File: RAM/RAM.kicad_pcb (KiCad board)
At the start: 2 copper layers, 133 x 58.5 mm, 60 parts, among them J1 Conn_01x02_Pin, J2 Conn_01x01_Pin, J3 Conn_01x02_Pin, J4 Conn_01x01_Pin, J5 Conn_01x05_Pin, J6 Conn_01x03_Pin, J7 Conn_01x03_Pin, J8 Conn_01x03_Pin, J9 Conn_01x10_Pin, U2 CD74HCT258E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

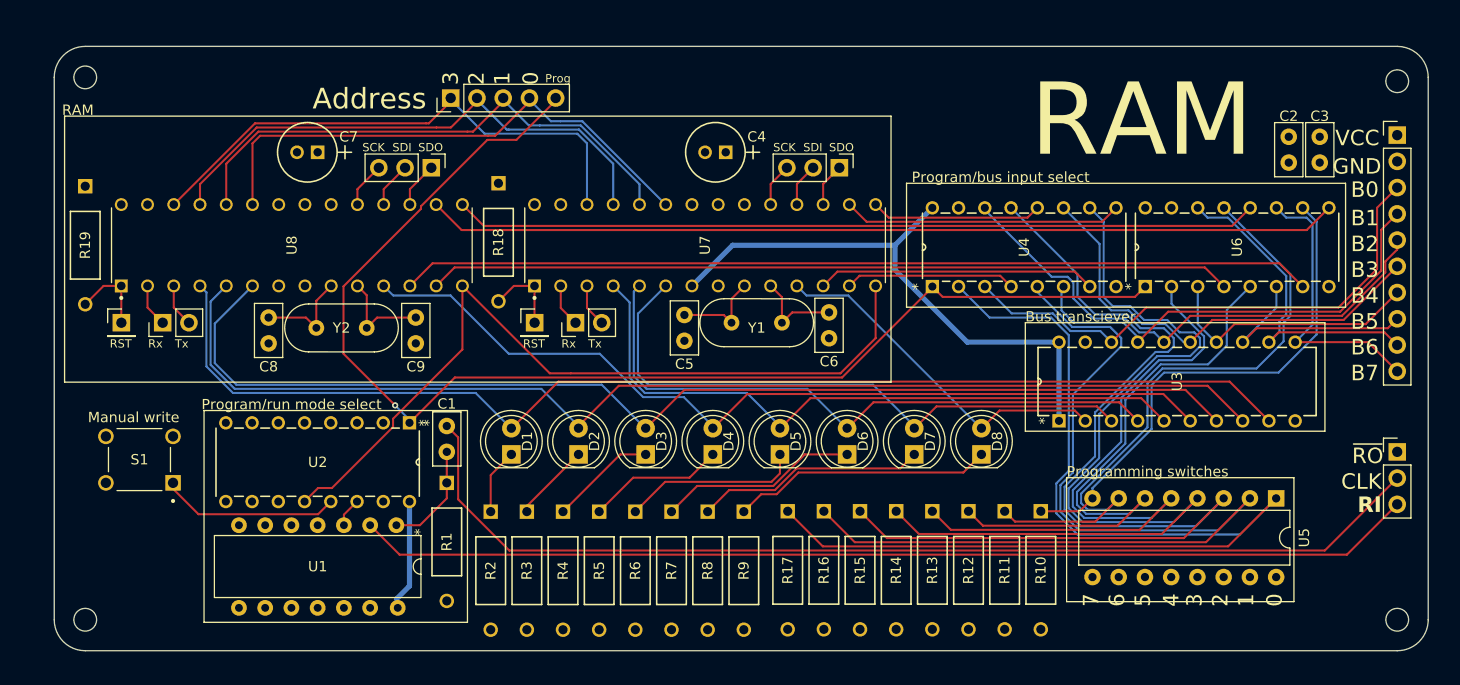
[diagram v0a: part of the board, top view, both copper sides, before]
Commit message: Reconnected ~RO. Cosmetic updates
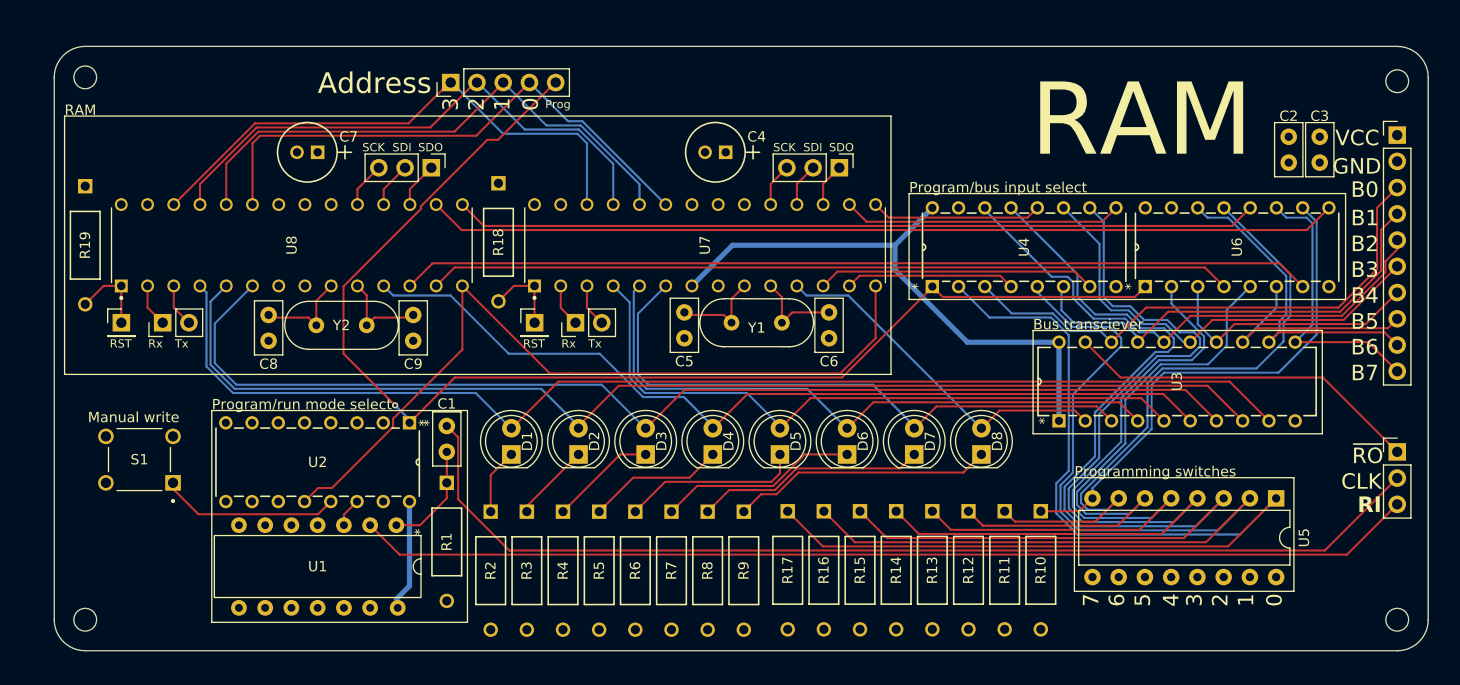
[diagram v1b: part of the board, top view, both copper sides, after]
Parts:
- moved J5 1.50 mm to (161.4, 41.2)
- moved C9 0.35 mm to (157.8, 66.2)
- moved C5 0.25 mm to (184.0, 63.5)
- moved C8 0.25 mm to (143.8, 63.8)
- moved Y2 0.25 mm to (150.8, 64.8)
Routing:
- net /~Read out: track 0.00 -> 34.6 mm
- net /A1: track 51.8 -> 53.3 mm
- net /A3: track 51.8 -> 53.3 mm
- net /A2: track 51.8 -> 53.3 mm
- net /A0: track 51.8 -> 53.3 mm
- net /AtmegaRamEmulatorB/XTAL2: track 9.60 -> 9.10 mm

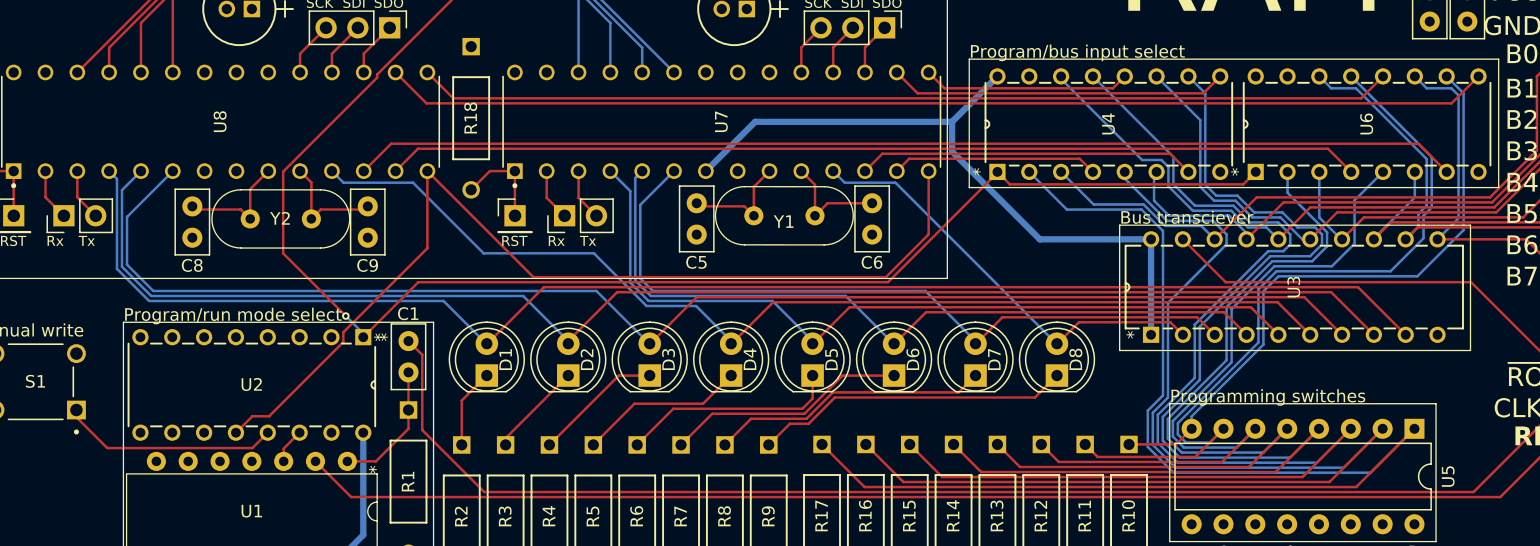
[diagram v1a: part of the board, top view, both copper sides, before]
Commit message: Fixed incorrect MUX inputs on RAM
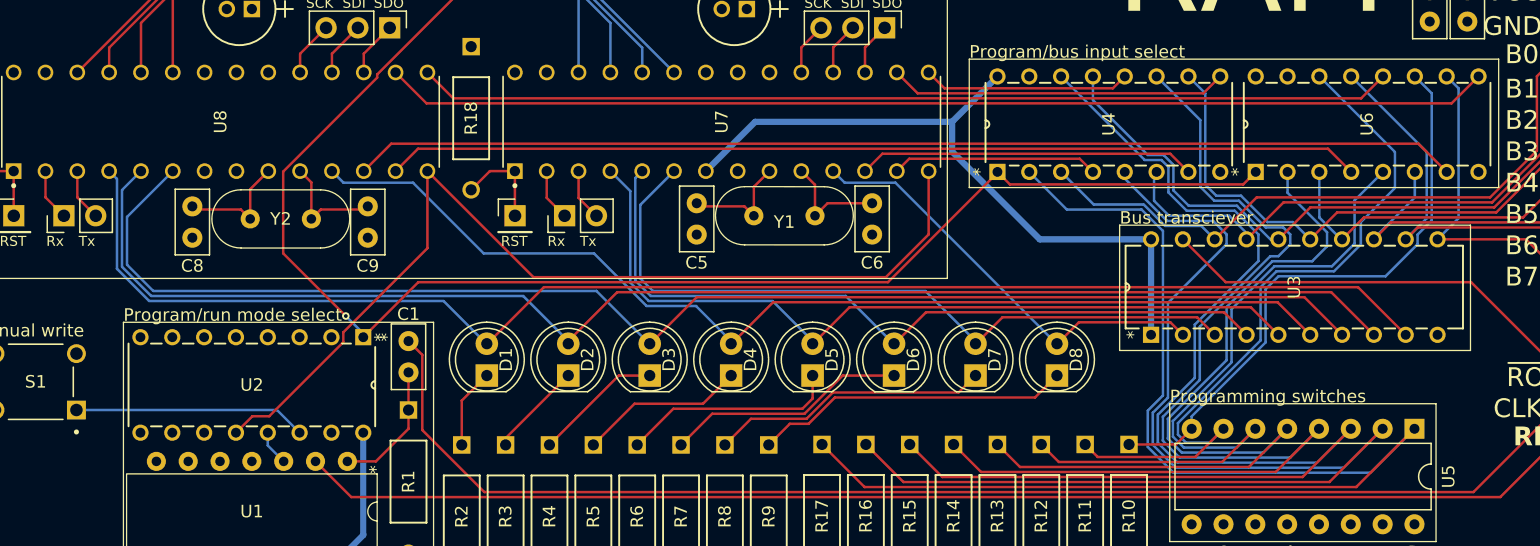
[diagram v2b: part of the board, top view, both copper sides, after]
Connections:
- R10 pad 2: +5V -> GND
- R11 pad 2: +5V -> GND
- R12 pad 2: +5V -> GND
- R13 pad 2: +5V -> GND
- R14 pad 2: +5V -> GND
- R15 pad 2: +5V -> GND
- R16 pad 2: +5V -> GND
- R17 pad 2: +5V -> GND
- S1 pad 1: Net-(U2-4A) -> Net-(U2-4B)
- U2 pad 13: Net-(U2-4A) -> Net-(U1-1Y)
- U2 pad 14: Net-(U1-1Y) -> Net-(U2-4B)
- U4 pad 10: /Prog 3 -> /Bus 3
- U4 pad 11: /Bus 3 -> /Prog 3
- U4 pad 13: /Prog 2 -> /Bus 2
- U4 pad 14: /Bus 2 -> /Prog 2
- U5 pad 10: GND -> +5V
- U5 pad 11: GND -> +5V
- U5 pad 12: GND -> +5V
- U5 pad 13: GND -> +5V
- U5 pad 14: GND -> +5V
- U5 pad 15: GND -> +5V
- U5 pad 16: GND -> +5V
- U5 pad 9: GND -> +5V
- U6 pad 10: /Prog 7 -> /Bus 7
- U6 pad 11: /Bus 7 -> /Prog 7
- U6 pad 13: /Prog 6 -> /Bus 6
- U6 pad 14: /Bus 6 -> /Prog 6
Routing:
- net Net-(U2-4B): track 0.00 -> 18.6 mm
- net Net-(U2-4A): track 17.4 -> 0.00 mm
- net /Prog 6: track 61.7 -> 57.7 mm
- net /Prog 3: track 89.2 -> 85.5 mm
- net /Prog 7: track 49.7 -> 47.1 mm
- net /Bus 6: track 31.7 -> 29.5 mm
- net /Bus 7: track 27.3 -> 25.1 mm
- net /Prog 2: track 99.0 -> 97.2 mm
- net /Bus 3: track 43.8 -> 42.5 mm
- net /Bus 2: track 51.6 -> 50.3 mm
- net Net-(U1-1Y): track 3.47 -> 2.82 mm
